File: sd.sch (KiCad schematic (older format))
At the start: 8 parts, among them J901 Micro_SD_Card_Det, U901 IP4220CZ6, U902 IP4220CZ6

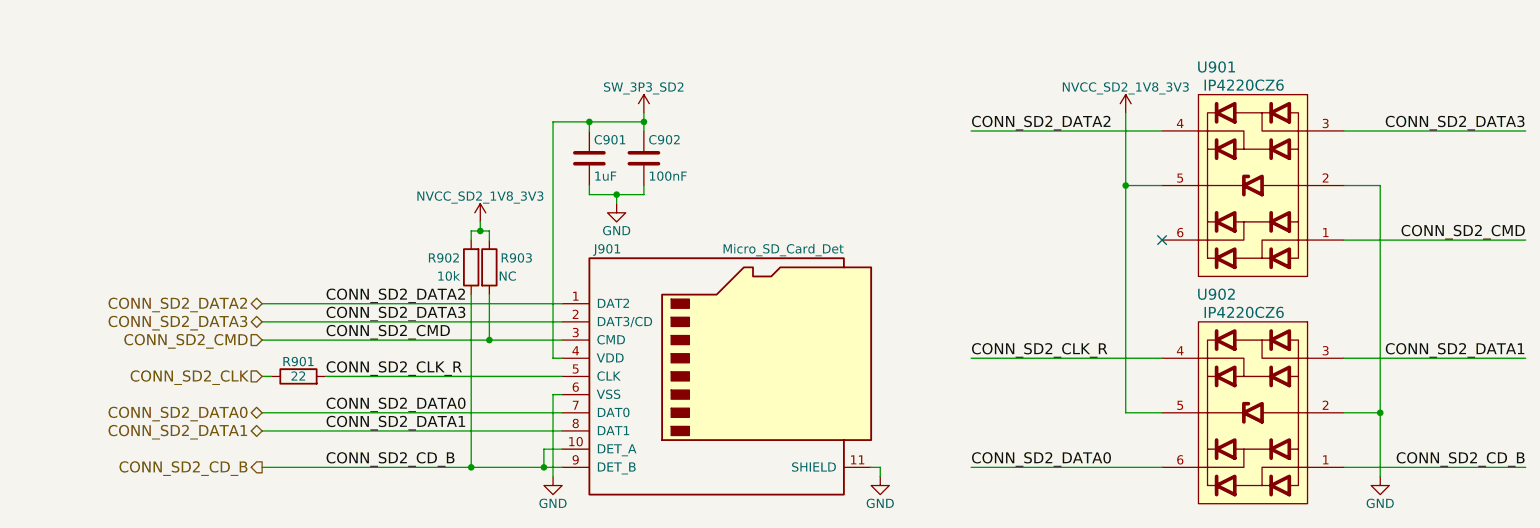
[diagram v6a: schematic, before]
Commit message: Modify the boot config pins such that the eMMC is an 8-bit bus, depressing a momentary push button switch during boot causes SD boot, and relevant options
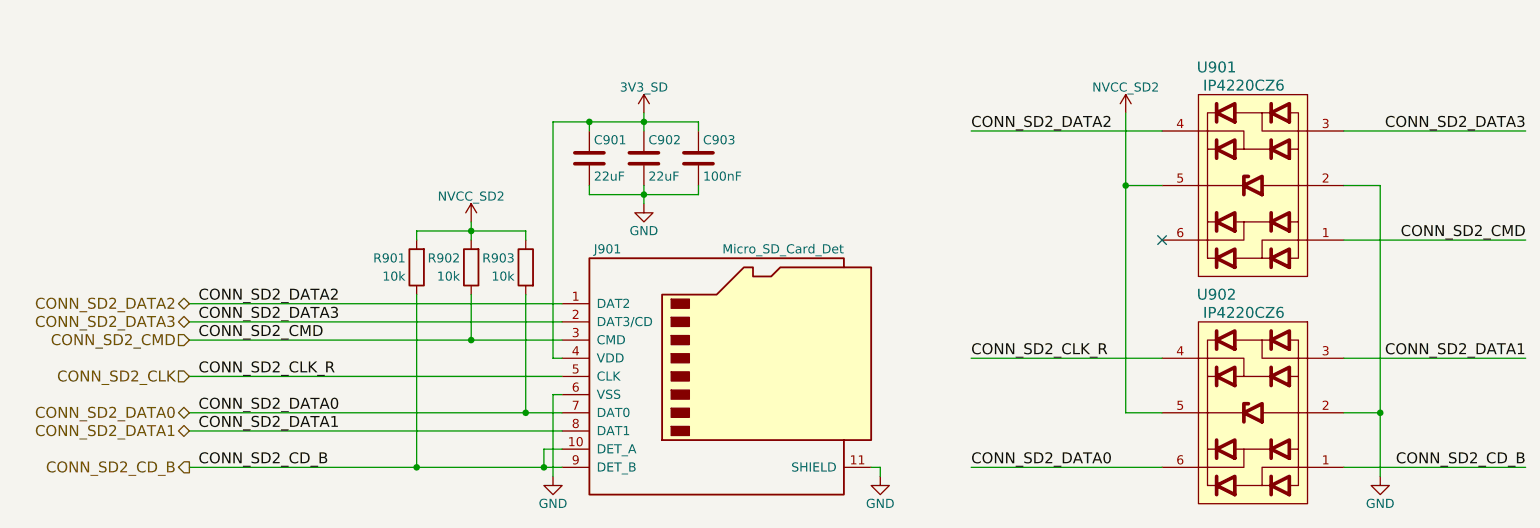
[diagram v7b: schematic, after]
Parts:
- added C903: 100nF, symbol C
- C901: value 1uF -> 22uF
- C902: value 100nF -> 22uF
- R901: value 22 -> 10k
- R903: value NC -> 10k
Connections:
- net CONN_SD2_CD_B: now also R901.1; no longer R902.1
- net CONN_SD2_CLK: now also J901.5 (CLK), U902.4; no longer R901.1
- net CONN_SD2_CMD: now also R902.1; no longer R903.2
- net CONN_SD2_DATA0: now also R903.2
- net GND: now also C903.2
- removed net CONN_SD2_CLK_R: J901.5 (CLK), R901.2, U902.4
- net NVCC_SD2_1V8_3V3 renamed NVCC_SD2
- net NVCC_SD2: now also R901.2
- net SW_3P3_SD2 renamed 3V3_SD
- net 3V3_SD: now also C903.1
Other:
- moved on the sheet: R903
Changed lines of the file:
@@
 	1    0    0    -1
 $EndComp
-Text HLabel 2250 4300 0    60   BiDi ~ 0
+Text HLabel 1850 4300 0    60   BiDi ~ 0
 CONN_SD2_DATA1
-Text HLabel 2250 4200 0    60   BiDi ~ 0
+Text HLabel 1850 4200 0    60   BiDi ~ 0
 CONN_SD2_DATA0
-Text HLabel 2250 3800 0    60   Input ~ 0
+Text HLabel 1850 3800 0    60   Input ~ 0
 CONN_SD2_CMD
-Text HLabel 2250 3700 0    60   BiDi ~ 0
+Text HLabel 1850 3700 0    60   BiDi ~ 0
 CONN_SD2_DATA3
-Text HLabel 2250 3600 0    60   BiDi ~ 0
+Text HLabel 1850 3600 0    60   BiDi ~ 0
 CONN_SD2_DATA2
-Text HLabel 2250 4000 0    60   Input ~ 0
+Text HLabel 1850 4000 0    60   Input ~ 0
 CONN_SD2_CLK
-Text HLabel 2250 4500 0    60   Output ~ 0
+Text HLabel 1850 4500 0    60   Output ~ 0
 CONN_SD2_CD_B
 $Comp
-L R R901
-U 1 1 5AC9FC3A
-P 2450 4000
-F 0 "R901" V 2530 4000 50  0000 C CNN
-F 1 "22" V 2450 4000 50  0000 C CNN
-F 2 "" V 2380 4000 50  0001 C CNN
-F 3 "" H 2450 4000 50  0001 C CNN
-	1    2450 4000
-	0    -1   -1   0
-$EndComp
-$Comp
-L GND #PWR0122
+L GND #PWR0119
 U 1 1 5AC9FCAE
 P 5650 4550
-F 0 "#PWR0122" H 5650 4300 50  0001 C CNN
+F 0 "#PWR0119" H 5650 4300 50  0001 C CNN
 F 1 "GND" H 5650 4400 50  0000 C CNN
 F 2 "" H 5650 4550 50  0001 C CNN
@@
 $EndComp
 $Comp
-L GND #PWR0123
+L GND #PWR0120
 U 1 1 5ACA0128
 P 3850 4550
-F 0 "#PWR0123" H 3850 4300 50  0001 C CNN
+F 0 "#PWR0120" H 3850 4300 50  0001 C CNN
 F 1 "GND" H 3850 4400 50  0000 C CNN
 F 2 "" H 3850 4550 50  0001 C CNN
@@
 L R R903
 U 1 1 5ACA05C1
-P 3500 3400
-F 0 "R903" H 3650 3450 50  0000 C CNN
-F 1 "NC" H 3600 3350 50  0000 C CNN
-F 2 "" V 3430 3400 50  0001 C CNN
-F 3 "" H 3500 3400 50  0001 C CNN
-	1    3500 3400
-	1    0    0    -1
+P 3700 3400
+F 0 "R903" H 3850 3450 50  0000 C CNN
+F 1 "10k" H 3825 3350 50  0000 C CNN
+F 2 "" V 3630 3400 50  0001 C CNN
+F 3 "" H 3700 3400 50  0001 C CNN
+	1    3700 3400
+	-1   0    0    -1
 $EndComp
 $Comp
@@
 P 4050 2800
 F 0 "C901" H 4075 2900 50  0000 L CNN
-F 1 "1uF" H 4075 2700 50  0000 L CNN
+F 1 "22uF" H 4075 2700 50  0000 L CNN
 F 2 "" H 4088 2650 50  0001 C CNN
 F 3 "" H 4050 2800 50  0001 C CNN
 	1    4050 2800
-	1    0    0    -1
-$EndComp
-$Comp
-L SW_3P3_SD2 #PWR0124
-U 1 1 5ACA0BF9
-P 4350 2550
-F 0 "#PWR0124" H 4350 2400 50  0001 C CNN
-F 1 "SW_3P3_SD2" H 4350 2690 50  0000 C CNN
-F 2 "" H 4350 2550 50  0001 C CNN
-F 3 "" H 4350 2550 50  0001 C CNN
-	1    4350 2550
-	1    0    0    -1
-$EndComp
-$Comp
-L NVCC_SD2_1V8_3V3 #PWR0125
-U 1 1 5ACA0C17
-P 3450 3150
-F 0 "#PWR0125" H 3450 3000 50  0001 C CNN
-F 1 "NVCC_SD2_1V8_3V3" H 3450 3290 50  0000 C CNN
-F 2 "" H 3450 3150 50  0001 C CNN
-F 3 "" H 3450 3150 50  0001 C CNN
-	1    3450 3150
 	1    0    0    -1
 $EndComp
@@
 P 4350 2800
 F 0 "C902" H 4375 2900 50  0000 L CNN
-F 1 "100nF" H 4375 2700 50  0000 L CNN
+F 1 "22uF" H 4375 2700 50  0000 L CNN
 F 2 "" H 4388 2650 50  0001 C CNN
 F 3 "" H 4350 2800 50  0001 C CNN
@@
 $EndComp
 $Comp
-L GND #PWR0126
+L GND #PWR0121
 U 1 1 5ACA12D0
-P 4200 3050
-F 0 "#PWR0126" H 4200 2800 50  0001 C CNN
-F 1 "GND" H 4200 2900 50  0000 C CNN
-F 2 "" H 4200 3050 50  0001 C CNN
-F 3 "" H 4200 3050 50  0001 C CNN
-	1    4200 3050
-	1    0    0    -1
-$EndComp
-Wire Wire Line
-	2250 3600 3900 3600
-Wire Wire Line
-	2250 3700 3900 3700
-Wire Wire Line
-	2250 3800 3900 3800
-Wire Wire Line
-	2250 4200 3900 4200
-Wire Wire Line
-	2250 4300 3900 4300
-Wire Wire Line
-	2250 4500 3900 4500
-Wire Wire Line
-	3900 4400 3800 4400
-Wire Wire Line
-	3800 4400 3800 4500
-Connection ~ 3800 4500
-Wire Wire Line
-	5650 4550 5650 4500
-Wire Wire Line
-	5650 4500 5600 4500
-Wire Wire Line
-	2250 4000 2300 4000
-Wire Wire Line
-	2600 4000 3900 4000
-Wire Wire Line
-	3850 4550 3850 4100
-Wire Wire Line
-	3850 4100 3900 4100
-Wire Wire Line
-	3400 3250 3400 3200
-Wire Wire Line
-	3500 3200 3500 3250
-Wire Wire Line
-	3400 3200 3500 3200
-Wire Wire Line
-	3450 3150 3450 3200
-Connection ~ 3450 3200
-Wire Wire Line
-	3850 3900 3850 2600
-Wire Wire Line
-	3850 2600 4350 2600
-Wire Wire Line
-	4350 2550 4350 2650
-Wire Wire Line
-	4050 2650 4050 2600
-Connection ~ 4050 2600
-Wire Wire Line
-	4050 2950 4050 3000
-Wire Wire Line
-	4050 3000 4350 3000
-Wire Wire Line
-	4350 3000 4350 2950
-Wire Wire Line
-	4200 3050 4200 3000
-Connection ~ 4200 3000
-Connection ~ 4350 2600
-Wire Wire Line
-	3400 3550 3400 4500
-Connection ~ 3400 4500
-Wire Wire Line
-	3500 3550 3500 3800
-Connection ~ 3500 3800
+P 4350 3050
+F 0 "#PWR0121" H 4350 2800 50  0001 C CNN
+F 1 "GND" H 4350 2900 50  0000 C CNN
+F 2 "" H 4350 3050 50  0001 C CNN
+F 3 "" H 4350 3050 50  0001 C CNN
+	1    4350 3050
+	1    0    0    -1
+$EndComp
 $Comp
 L IP4220CZ6 U901
@@
 NoConn ~ 7200 3250
 $Comp
-L GND #PWR0127
+L GND #PWR0122
 U 1 1 5ACB9D67
 P 8400 4550
-F 0 "#PWR0127" H 8400 4300 50  0001 C CNN
+F 0 "#PWR0122" H 8400 4300 50  0001 C CNN
 F 1 "GND" H 8400 4400 50  0000 C CNN
 F 2 "" H 8400 4550 50  0001 C CNN
@@
 	1    0    0    -1
 $EndComp
-Wire Wire Line
-	8400 2950 8400 4550
-Wire Wire Line
-	8400 4200 8200 4200
-Wire Wire Line
-	8400 2950 8200 2950
-Connection ~ 8400 4200
-$Comp
-L NVCC_SD2_1V8_3V3 #PWR0128
-U 1 1 5ACB9F80
-P 7000 2550
-F 0 "#PWR0128" H 7000 2400 50  0001 C CNN
-F 1 "NVCC_SD2_1V8_3V3" H 7000 2690 50  0000 C CNN
-F 2 "" H 7000 2550 50  0001 C CNN
-F 3 "" H 7000 2550 50  0001 C CNN
-	1    7000 2550
-	1    0    0    -1
-$EndComp
-Wire Wire Line
-	7000 2550 7000 4200
-Wire Wire Line
-	7000 4200 7200 4200
-Wire Wire Line
-	7200 2950 7000 2950
-Connection ~ 7000 2950
 Text Label 6150 2650 0    60   ~ 0
 CONN_SD2_DATA2
-Wire Wire Line
-	7200 2650 6150 2650
 Text Label 9200 2650 2    60   ~ 0
 CONN_SD2_DATA3
-Wire Wire Line
-	8200 2650 9200 2650
 Text Label 9200 3250 2    60   ~ 0
 CONN_SD2_CMD
-Wire Wire Line
-	8200 3250 9200 3250
 Text Label 9200 3900 2    60   ~ 0
 CONN_SD2_DATA1
-Wire Wire Line
-	8200 3900 9200 3900
 Text Label 9200 4500 2    60   ~ 0
 CONN_SD2_CD_B
-Wire Wire Line
-	8200 4500 9200 4500
 Text Label 6150 3900 0    60   ~ 0
 CONN_SD2_CLK_R
 Text Label 6150 4500 0    60   ~ 0
 CONN_SD2_DATA0
+Text Label 1900 3600 0    60   ~ 0
+CONN_SD2_DATA2
+Text Label 1900 4000 0    60   ~ 0
+CONN_SD2_CLK_R
+Text Label 1900 4200 0    60   ~ 0
+CONN_SD2_DATA0
+Text Label 1900 3700 0    60   ~ 0
+CONN_SD2_DATA3
+Text Label 1900 3800 0    60   ~ 0
+CONN_SD2_CMD
+Text Label 1900 4300 0    60   ~ 0
+CONN_SD2_DATA1
+Text Label 1900 4500 0    60   ~ 0
+CONN_SD2_CD_B
+$Comp
+L NVCC_SD2 #PWR0123
+U 1 1 5AE77A2E
+P 3400 3150
+F 0 "#PWR0123" H 3400 3000 50  0001 C CNN
+F 1 "NVCC_SD2" H 3400 3290 50  0000 C CNN
+F 2 "" H 3400 3150 50  0001 C CNN
+F 3 "" H 3400 3150 50  0001 C CNN
+	1    3400 3150
+	1    0    0    -1
+$EndComp
+$Comp
+L NVCC_SD2 #PWR0124
+U 1 1 5AE85069
+P 7000 2550
+F 0 "#PWR0124" H 7000 2400 50  0001 C CNN
+F 1 "NVCC_SD2" H 7000 2690 50  0000 C CNN
+F 2 "" H 7000 2550 50  0001 C CNN
+F 3 "" H 7000 2550 50  0001 C CNN
+	1    7000 2550
+	1    0    0    -1
+$EndComp
+$Comp
+L 3V3_SD #PWR0125
+U 1 1 5AE8C9A8
+P 4350 2550
+F 0 "#PWR0125" H 4350 2400 50  0001 C CNN
+F 1 "3V3_SD" H 4350 2690 50  0000 C CNN
+F 2 "" H 4350 2550 50  0001 C CNN
+F 3 "" H 4350 2550 50  0001 C CNN
+	1    4350 2550
+	1    0    0    -1
+$EndComp
+$Comp
+L C C903
+U 1 1 5AE8CA13
+P 4650 2800
+F 0 "C903" H 4675 2900 50  0000 L CNN
+F 1 "100nF" H 4675 2700 50  0000 L CNN
+F 2 "" H 4688 2650 50  0001 C CNN
+F 3 "" H 4650 2800 50  0001 C CNN
+	1    4650 2800
+	1    0    0    -1
+$EndComp
+$Comp
+L R R901
+U 1 1 5AE8F616
+P 3100 3400
+F 0 "R901" H 3250 3350 50  0000 C CNN
+F 1 "10k" H 3225 3450 50  0000 C CNN
+F 2 "" V 3030 3400 50  0001 C CNN
+F 3 "" H 3100 3400 50  0001 C CNN
+	1    3100 3400
+	-1   0    0    1
+$EndComp
+Connection ~ 3700 4200
+Wire Wire Line
+	3700 3550 3700 4200
+Wire Wire Line
+	3100 3200 3700 3200
+Wire Wire Line
+	3100 3250 3100 3200
+Wire Wire Line
+	3400 3150 3400 3250
+Connection ~ 4350 3000
+Wire Wire Line
+	4350 2950 4350 3050
+Wire Wire Line
+	4050 3000 4650 3000
+Wire Wire Line
+	4650 3000 4650 2950
+Wire Wire Line
+	4650 2600 4650 2650
+Wire Wire Line
+	3850 3900 3900 3900
+Wire Wire Line
+	7200 3900 6150 3900
 Wire Wire Line
 	7200 4500 6150 4500
 Wire Wire Line
-	7200 3900 6150 3900
-Text Label 2600 3600 0    60   ~ 0
-CONN_SD2_DATA2
-Text Label 2600 4000 0    60   ~ 0
-CONN_SD2_CLK_R
-Text Label 2600 4200 0    60   ~ 0
-CONN_SD2_DATA0
-Text Label 2600 3700 0    60   ~ 0
-CONN_SD2_DATA3
-Text Label 2600 3800 0    60   ~ 0
-CONN_SD2_CMD
-Text Label 2600 4300 0    60   ~ 0
-CONN_SD2_DATA1
-Text Label 2600 4500 0    60   ~ 0
-CONN_SD2_CD_B
-Wire Wire Line
-	3850 3900 3900 3900
+	8200 4500 9200 4500
+Wire Wire Line
+	8200 3900 9200 3900
+Wire Wire Line
+	8200 3250 9200 3250
+Wire Wire Line
+	8200 2650 9200 2650
+Wire Wire Line
+	7200 2650 6150 2650
+Connection ~ 7000 2950
+Wire Wire Line
+	7200 2950 7000 2950
+Wire Wire Line
+	7000 4200 7200 4200
+Wire Wire Line
+	7000 2550 7000 4200
+Connection ~ 8400 4200
+Wire Wire Line
+	8400 2950 8200 2950
+Wire Wire Line
+	8400 4200 8200 4200
+Wire Wire Line
+	8400 2950 8400 4550
+Connection ~ 4350 2600
+Wire Wire Line
+	4050 2950 4050 3000
+Connection ~ 4050 2600
+Wire Wire Line
+	4050 2650 4050 2600
+Wire Wire Line
+	4350 2550 4350 2650
+Wire Wire Line
+	3850 2600 4650 2600
+Wire Wire Line
+	3850 3900 3850 2600
+Connection ~ 3400 3200
+Wire Wire Line
+	3700 3200 3700 3250
+Wire Wire Line
+	3850 4100 3900 4100
+Wire Wire Line
+	3850 4550 3850 4100
+Wire Wire Line
+	1850 4000 3900 4000
+Wire Wire Line
+	5650 4500 5600 4500
+Wire Wire Line
+	5650 4550 5650 4500
+Connection ~ 3800 4500
+Wire Wire Line
+	3800 4400 3800 4500
+Wire Wire Line
+	3900 4400 3800 4400
+Wire Wire Line
+	1850 4300 3900 4300
+Wire Wire Line
+	1850 4200 3900 4200
+Wire Wire Line
+	1850 3800 3900 3800
+Wire Wire Line
+	1850 3700 3900 3700
+Wire Wire Line
+	1850 3600 3900 3600
+Wire Wire Line
+	1850 4500 3900 4500
+Wire Wire Line
+	3400 3550 3400 3800
+Connection ~ 3400 3800
+Wire Wire Line
+	3100 3550 3100 4500
+Connection ~ 3100 4500
 $EndSCHEMATC

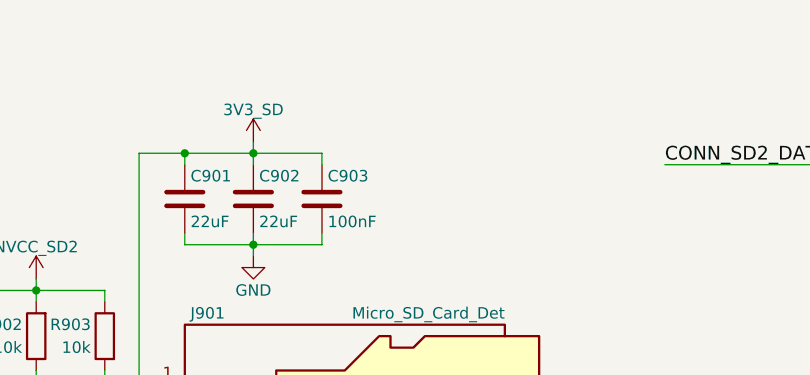
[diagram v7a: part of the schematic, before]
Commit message: Begin USB 2.0 hub circuit for M.2 modules, remove supervisory/voltage monitor/watchdog circuit since the EmCraft SoM implements it
USB 2.0 hub circuit still needs to be completed.
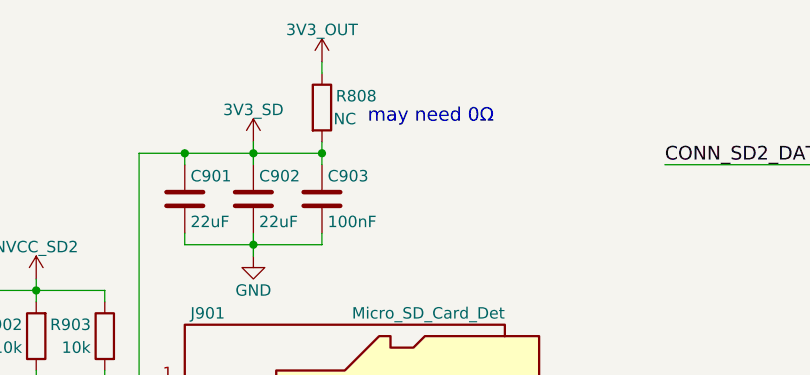
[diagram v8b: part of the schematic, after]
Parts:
- added R808: NC, symbol R
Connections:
- net 3V3_SD: now also R808.2
- new net 3V3_OUT: R808.1
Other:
- note added: "may need 0Ω"
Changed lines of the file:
@@
 $Descr A4 11693 8268
 encoding utf-8
-Sheet 9 15
+Sheet 8 14
 Title "uSD Card"
 Date "2018-04-19"
@@
 CONN_SD2_CD_B
 $Comp
-L GND #PWR0119
+L GND #PWR0113
 U 1 1 5AC9FCAE
 P 5650 4550
-F 0 "#PWR0119" H 5650 4300 50  0001 C CNN
+F 0 "#PWR0113" H 5650 4300 50  0001 C CNN
 F 1 "GND" H 5650 4400 50  0000 C CNN
 F 2 "" H 5650 4550 50  0001 C CNN
@@
 $EndComp
 $Comp
-L GND #PWR0120
+L GND #PWR0114
 U 1 1 5ACA0128
 P 3850 4550
-F 0 "#PWR0120" H 3850 4300 50  0001 C CNN
+F 0 "#PWR0114" H 3850 4300 50  0001 C CNN
 F 1 "GND" H 3850 4400 50  0000 C CNN
 F 2 "" H 3850 4550 50  0001 C CNN
@@
 $EndComp
 $Comp
-L GND #PWR0121
+L GND #PWR0115
 U 1 1 5ACA12D0
 P 4350 3050
-F 0 "#PWR0121" H 4350 2800 50  0001 C CNN
+F 0 "#PWR0115" H 4350 2800 50  0001 C CNN
 F 1 "GND" H 4350 2900 50  0000 C CNN
 F 2 "" H 4350 3050 50  0001 C CNN
@@
 NoConn ~ 7200 3250
 $Comp
-L GND #PWR0122
+L GND #PWR0116
 U 1 1 5ACB9D67
 P 8400 4550
-F 0 "#PWR0122" H 8400 4300 50  0001 C CNN
+F 0 "#PWR0116" H 8400 4300 50  0001 C CNN
 F 1 "GND" H 8400 4400 50  0000 C CNN
 F 2 "" H 8400 4550 50  0001 C CNN
@@
 CONN_SD2_CD_B
 $Comp
-L NVCC_SD2 #PWR0123
+L NVCC_SD2 #PWR0117
 U 1 1 5AE77A2E
 P 3400 3150
-F 0 "#PWR0123" H 3400 3000 50  0001 C CNN
+F 0 "#PWR0117" H 3400 3000 50  0001 C CNN
 F 1 "NVCC_SD2" H 3400 3290 50  0000 C CNN
 F 2 "" H 3400 3150 50  0001 C CNN
@@
 $EndComp
 $Comp
-L NVCC_SD2 #PWR0124
+L NVCC_SD2 #PWR0118
 U 1 1 5AE85069
 P 7000 2550
-F 0 "#PWR0124" H 7000 2400 50  0001 C CNN
+F 0 "#PWR0118" H 7000 2400 50  0001 C CNN
 F 1 "NVCC_SD2" H 7000 2690 50  0000 C CNN
 F 2 "" H 7000 2550 50  0001 C CNN
@@
 $EndComp
 $Comp
-L 3V3_SD #PWR0125
+L 3V3_SD #PWR0119
 U 1 1 5AE8C9A8
 P 4350 2550
-F 0 "#PWR0125" H 4350 2400 50  0001 C CNN
+F 0 "#PWR0119" H 4350 2400 50  0001 C CNN
 F 1 "3V3_SD" H 4350 2690 50  0000 C CNN
 F 2 "" H 4350 2550 50  0001 C CNN
@@
 	4650 3000 4650 2950
 Wire Wire Line
-	4650 2600 4650 2650
+	4650 2550 4650 2650
 Wire Wire Line
 	3850 3900 3900 3900
@@
 	3100 3550 3100 4500
 Connection ~ 3100 4500
+$Comp
+L R R808
+U 1 1 5AF7AE7F
+P 4650 2400
+F 0 "R808" H 4800 2450 50  0000 C CNN
+F 1 "NC" H 4750 2350 50  0000 C CNN
+F 2 "" V 4580 2400 50  0001 C CNN
+F 3 "" H 4650 2400 50  0001 C CNN
+	1    4650 2400
+	1    0    0    -1
+$EndComp
+$Comp
+L 3V3_OUT #PWR0120
+U 1 1 5AF7AED2
+P 4650 2200
+F 0 "#PWR0120" H 4650 2050 50  0001 C CNN
+F 1 "3V3_OUT" H 4650 2340 50  0000 C CNN
+F 2 "" H 4650 2200 50  0001 C CNN
+F 3 "" H 4650 2200 50  0001 C CNN
+	1    4650 2200
+	1    0    0    -1
+$EndComp
+Connection ~ 4650 2600
+Wire Wire Line
+	4650 2250 4650 2200
+Text Notes 4850 2475 0    60   ~ 0
+may need 0Ω
 $EndSCHEMATC
